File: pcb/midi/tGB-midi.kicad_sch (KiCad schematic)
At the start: 25 parts, among them J1 MIDI_IN, J2 MIDI_THRU, J3 MIDI_OUT, J4 IO, U1 TLP2368, U2 TC7WZ07FK

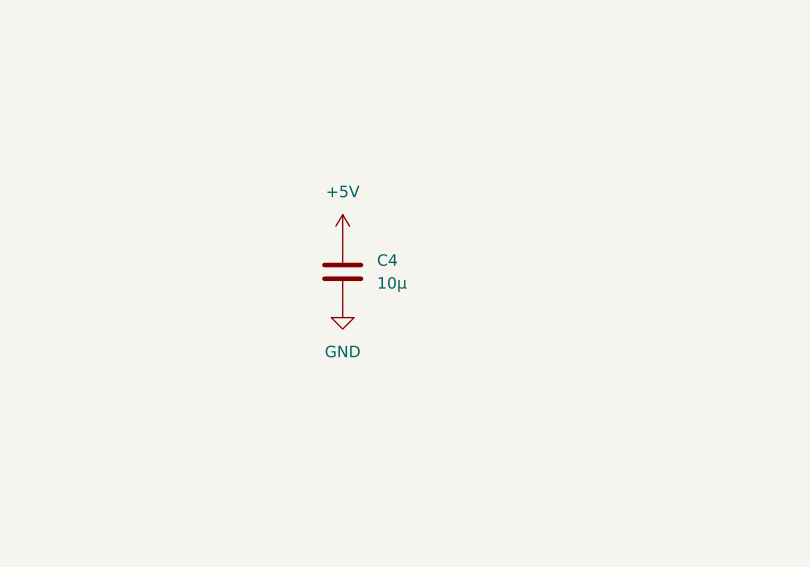
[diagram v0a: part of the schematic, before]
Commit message: change C4 value from 10uF to 4.7uF
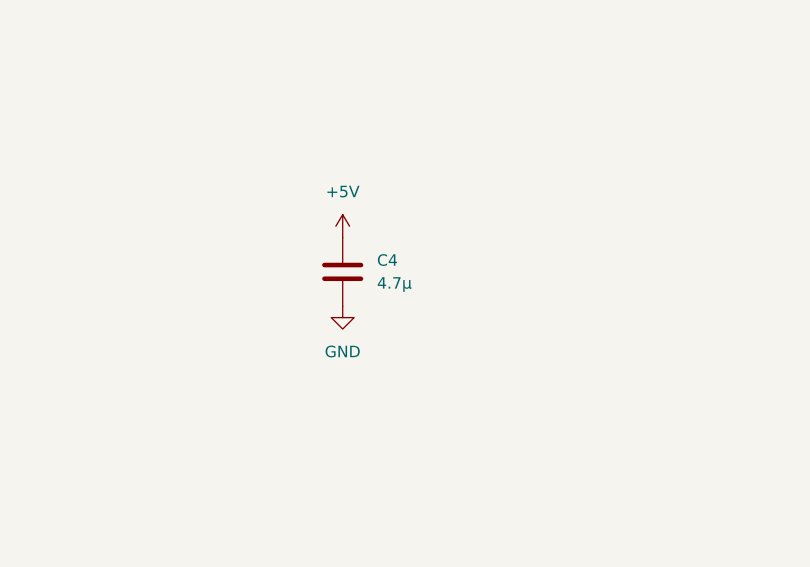
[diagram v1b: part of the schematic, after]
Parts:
- C4: value 10μ -> 4.7μ
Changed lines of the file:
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@@
       (effects (font (size 1.27 1.27)) (justify left))
     )
-    (property "Value" "10μ" (id 1) (at 245.11 59.6899 0)
+    (property "Value" "4.7μ" (id 1) (at 245.11 59.6899 0)
       (effects (font (size 1.27 1.27)) (justify left))
     )
@@
     )
     (path "/165b2782-2d75-4312-85a0-80e5d9d4ff9f"
-      (reference "C4") (unit 1) (value "10μ") (footprint "Capacitor_SMD:C_0402_1005Metric")
+      (reference "C4") (unit 1) (value "4.7μ") (footprint "Capacitor_SMD:C_0402_1005Metric")
     )
     (path "/cfbbba51-0adb-4b5c-a79a-58d8e2b466b2"

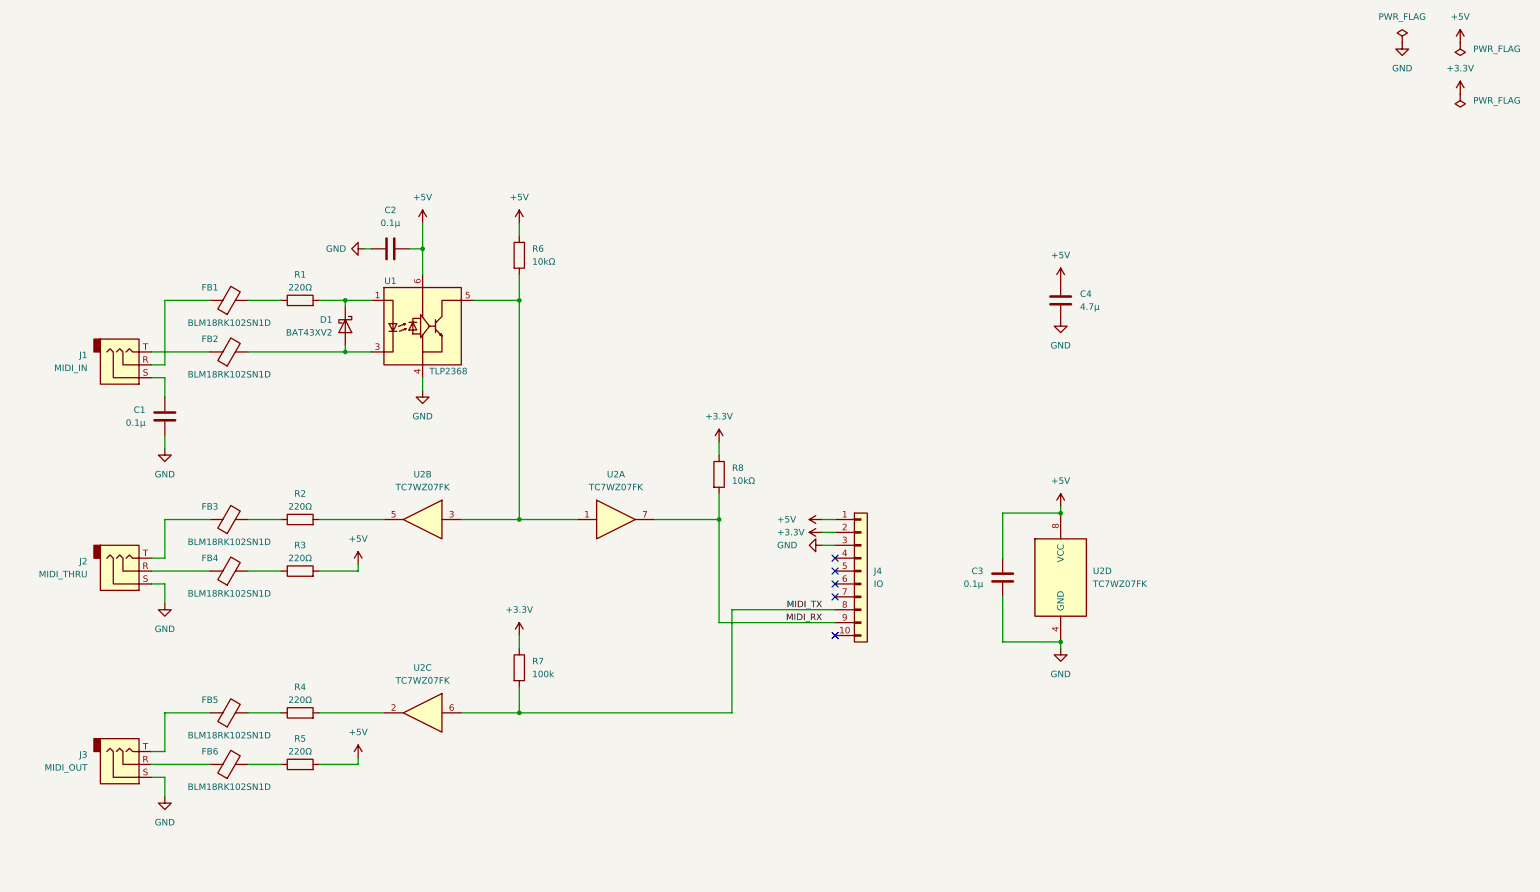
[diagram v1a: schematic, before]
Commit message: add comment, fix power net name
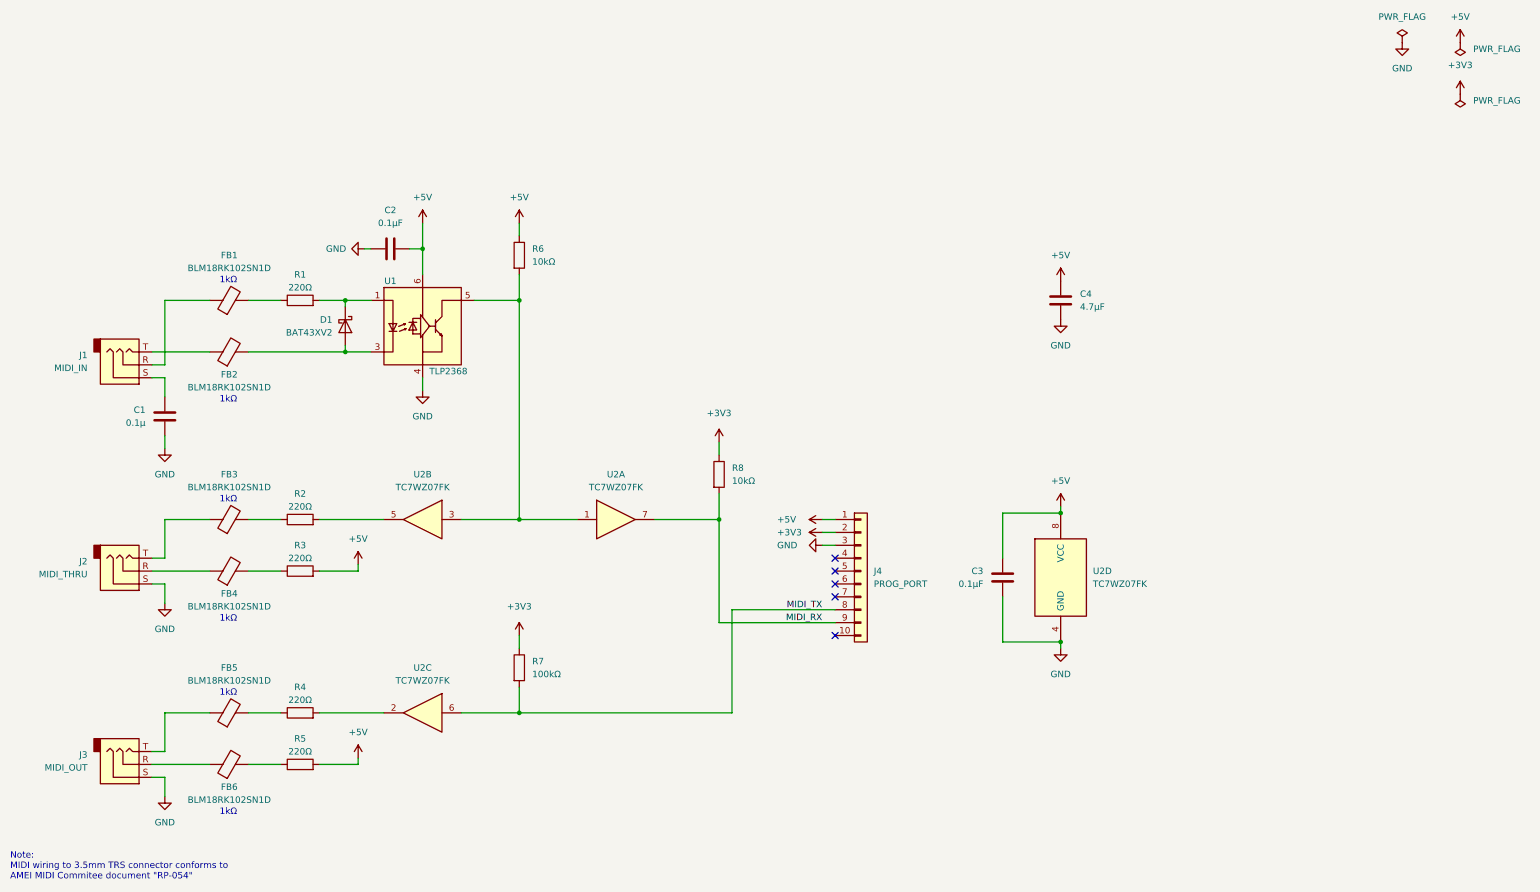
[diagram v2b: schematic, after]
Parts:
- C2, C3: value 0.1μ -> 0.1μF
- C4: value 4.7μ -> 4.7μF
- J4: value IO -> PROG_PORT
- R7: value 100k -> 100kΩ
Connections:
- net +3.3V renamed +3V3
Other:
- note added: "1kΩ"
- note added: "Note: MIDI wiring to 3.5mm TRS connector conforms to AMEI MIDI Commitee document "RP-054""

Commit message: set title and revision
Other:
- title: (none) -> tsuraraGB MIDI Adapter PCB
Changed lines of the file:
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@@
 (kicad_sch (version 20211123) (generator eeschema)
   (paper "A4")
+  (title_block
+    (title "tsuraraGB MIDI Adapter PCB")
+    (rev "A")
+  )
   (junction (at 134.62 101.6) (diameter 0) (color 0 0 0 0)
   )

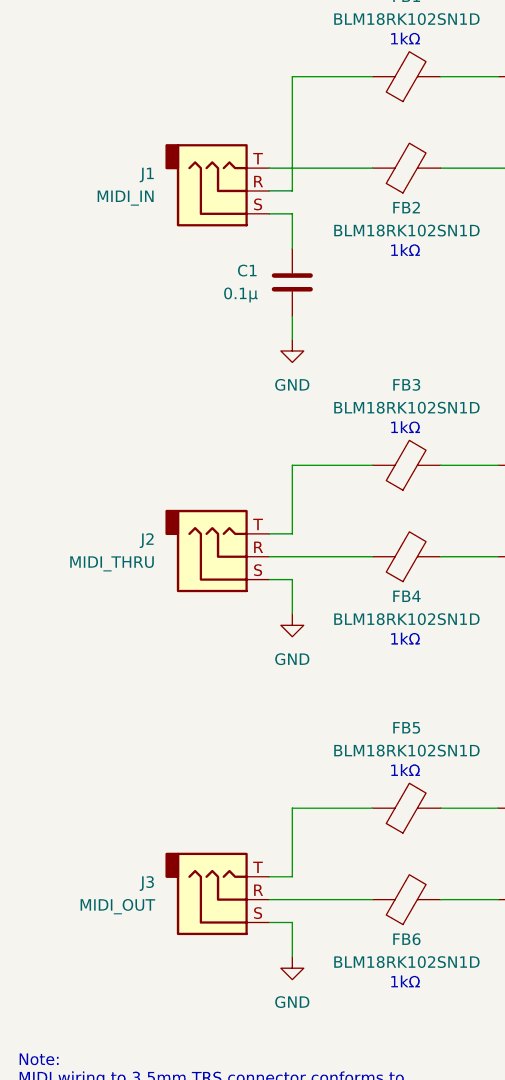
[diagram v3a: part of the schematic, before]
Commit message: migration from KiCad 6 to 7
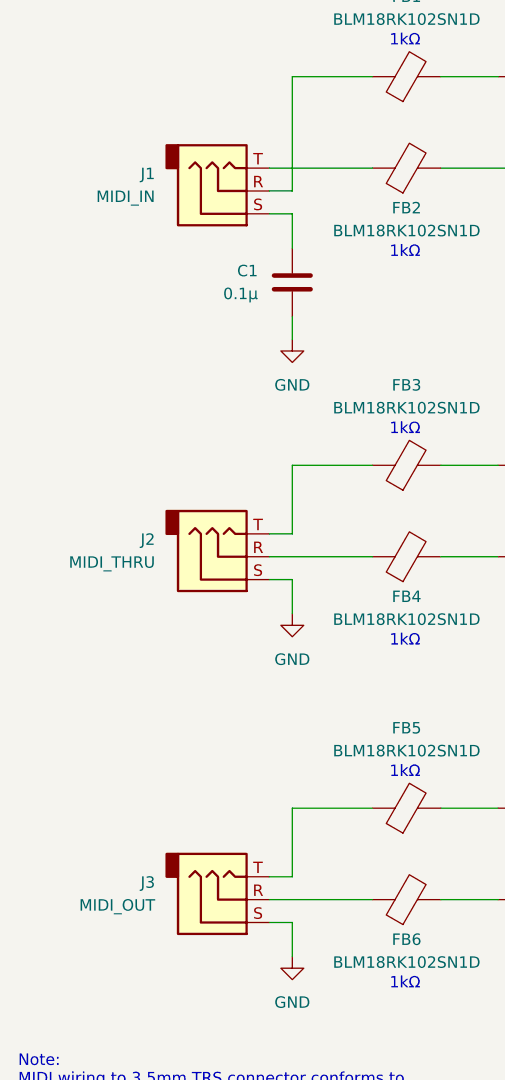
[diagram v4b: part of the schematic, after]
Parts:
- J1, J2, J3: symbol Connector:AudioJack3 -> Connector_Audio:AudioJack3

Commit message: migrate KiCad 7 -> 10
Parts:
- J1, J2, J3: footprint MJ-8435:MJ-8435 -> ProjectSpecific:MJ-8435
- J4: footprint Pin_Sidemount:PinSocket_1x10_P2.54_Sidemount -> ProjectSpecific:PinSocket_1x10_P2.54_Sidemount
- U1: footprint Package_SO:SO-5_4.4x3.6mm_P1.27mm -> ProjectSpecific:SO-5_4.4x3.6mm_P1.27mm; symbol Isolator:TLP2768A -> ProjectSpecific:TLP2368
- U2: footprint Package_SO:VSSOP-8_2.3x2mm_P0.5mm -> ProjectSpecific:VSSOP-8_2.3x2mm_P0.5mm
